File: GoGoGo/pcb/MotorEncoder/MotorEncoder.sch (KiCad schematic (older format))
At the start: 7 parts

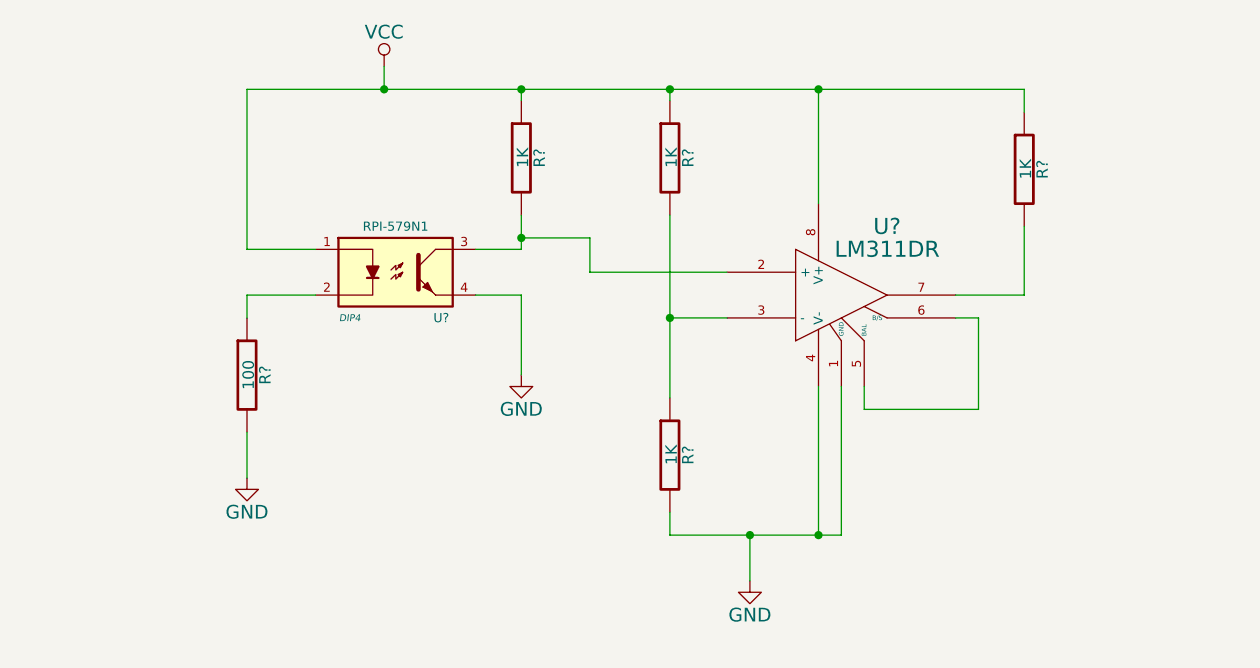
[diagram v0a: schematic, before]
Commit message: GGG MotorEncoder schematic updated with missing video items
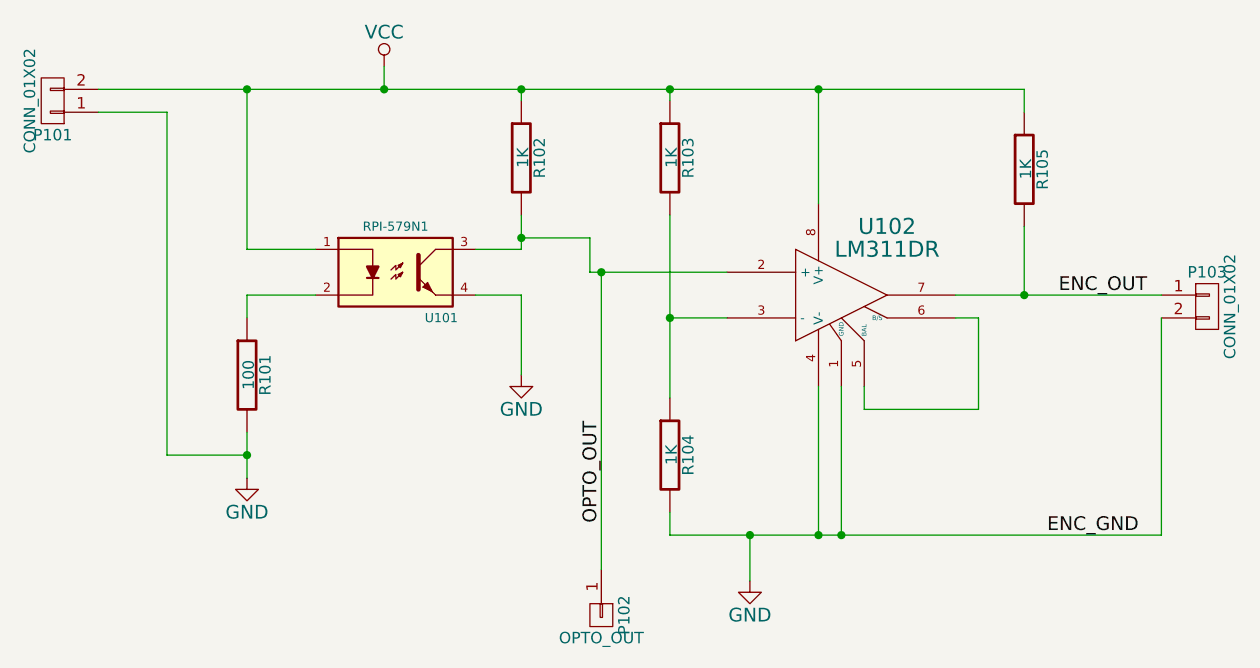
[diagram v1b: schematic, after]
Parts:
- added P101, P103: CONN_01X02, symbol CONN_01X02
- added P102: OPTO_OUT, symbol CONN_01X01
- R101, R102, R103, R104, R105: renamed from R?; footprint (none) -> Resistors_SMD:R_0805_HandSoldering
- U101: renamed from U?; footprint DIP4 -> (none)
- gave numbers to parts that had none: 1
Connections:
- net GND: now also P101.1 (P1), P103.2 (P2)
- net VCC: now also P101.2 (P2)
- net OPTO_OUT: now reaches R102.2, U101.3, U102.2 (+)
- net OPTO_OUT: now also P102.1 (P1)
- net ENC_OUT: now reaches R105.2, U102.7
- net ENC_OUT: now also P103.1 (P1)
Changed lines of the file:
@@
 $EndDescr
 $Comp
-L RPI-579N1 U?
+L RPI-579N1 U101
 U 1 1 55B03B5A
 P 5550 3350
-F 0 "U?" H 5750 3150 40  0000 C CNN
+F 0 "U101" H 5750 3150 40  0000 C CNN
 F 1 "RPI-579N1" H 5550 3550 40  0000 C CNN
-F 2 "DIP4" H 5350 3150 30  0000 C CIN
+F 2 "" H 5350 3150 30  0000 C CIN
 F 3 "" H 5550 3350 60  0000 C CNN
 	1    5550 3350
@@
 $EndComp
 $Comp
-L R R?
+L R R101
 U 1 1 55B03C1A
 P 4900 3800
-F 0 "R?" V 4980 3800 50  0000 C CNN
+F 0 "R101" V 4980 3800 50  0000 C CNN
 F 1 "100" V 4907 3801 50  0000 C CNN
-F 2 "" V 4830 3800 30  0000 C CNN
+F 2 "Resistors_SMD:R_0805_HandSoldering" V 4830 3800 30  0001 C CNN
 F 3 "" H 4900 3800 30  0000 C CNN
 	1    4900 3800
@@
 $EndComp
 $Comp
-L VCC #PWR?
+L VCC #PWR102
 U 1 1 55B03C53
 P 5500 2450
-F 0 "#PWR?" H 5500 2300 60  0001 C CNN
+F 0 "#PWR102" H 5500 2300 60  0001 C CNN
 F 1 "VCC" H 5500 2600 60  0000 C CNN
 F 2 "" H 5500 2450 60  0000 C CNN
@@
 $EndComp
 $Comp
-L GND #PWR?
+L GND #PWR101
 U 1 1 55B03C96
 P 4900 4250
-F 0 "#PWR?" H 4900 4000 60  0001 C CNN
+F 0 "#PWR101" H 4900 4000 60  0001 C CNN
 F 1 "GND" H 4900 4100 60  0000 C CNN
 F 2 "" H 4900 4250 60  0000 C CNN
@@
 $EndComp
 $Comp
-L GND #PWR?
+L GND #PWR103
 U 1 1 55B03CB8
 P 6100 3800
-F 0 "#PWR?" H 6100 3550 60  0001 C CNN
+F 0 "#PWR103" H 6100 3550 60  0001 C CNN
 F 1 "GND" H 6100 3650 60  0000 C CNN
 F 2 "" H 6100 3800 60  0000 C CNN
@@
 $EndComp
 $Comp
-L LM311N U?
+L LM311N U102
 U 1 1 55B040EE
 P 7500 3450
-F 0 "U?" H 7700 3750 70  0000 C CNN
+F 0 "U102" H 7700 3750 70  0000 C CNN
 F 1 "LM311DR" H 7700 3650 70  0000 C CNN
-F 2 "" H 7500 3450 60  0000 C CNN
+F 2 "" H 7500 3450 60  0001 C CNN
 F 3 "" H 7500 3450 60  0000 C CNN
 	1    7500 3450
@@
 	6100 3250 6100 3100
 Wire Wire Line
-	4900 2550 8300 2550
+	4250 2550 8300 2550
 Wire Wire Line
 	6100 2550 6100 2600
@@
 Connection ~ 6100 2550
 $Comp
-L R R?
+L R R103
 U 1 1 55B04354
 P 6750 2850
-F 0 "R?" V 6830 2850 50  0000 C CNN
+F 0 "R103" V 6830 2850 50  0000 C CNN
 F 1 "1K" V 6757 2851 50  0000 C CNN
-F 2 "" V 6680 2850 30  0000 C CNN
+F 2 "Resistors_SMD:R_0805_HandSoldering" V 6680 2850 30  0001 C CNN
 F 3 "" H 6750 2850 30  0000 C CNN
 	1    6750 2850
@@
 	6750 3550 7000 3550
 $Comp
-L R R?
+L R R104
 U 1 1 55B043E5
 P 6750 4150
-F 0 "R?" V 6830 4150 50  0000 C CNN
+F 0 "R104" V 6830 4150 50  0000 C CNN
 F 1 "1K" V 6757 4151 50  0000 C CNN
-F 2 "" V 6680 4150 30  0000 C CNN
+F 2 "Resistors_SMD:R_0805_HandSoldering" V 6680 4150 30  0001 C CNN
 F 3 "" H 6750 4150 30  0000 C CNN
 	1    6750 4150
@@
 Connection ~ 7400 2550
 Wire Wire Line
-	8000 3450 8300 3450
-$Comp
-L R R?
+	8000 3450 8900 3450
+$Comp
+L R R105
 U 1 1 55B044E9
 P 8300 2900
-F 0 "R?" V 8380 2900 50  0000 C CNN
+F 0 "R105" V 8380 2900 50  0000 C CNN
 F 1 "1K" V 8307 2901 50  0000 C CNN
-F 2 "" V 8230 2900 30  0000 C CNN
+F 2 "Resistors_SMD:R_0805_HandSoldering" V 8230 2900 30  0001 C CNN
 F 3 "" H 8300 2900 30  0000 C CNN
 	1    8300 2900
@@
 	6750 4400 6750 4500
 Wire Wire Line
-	6750 4500 7500 4500
+	6750 4500 8900 4500
 Wire Wire Line
 	7500 4500 7500 3850
@@
 Connection ~ 7100 4500
 $Comp
-L GND #PWR?
+L GND #PWR104
 U 1 1 55B046A7
 P 7100 4700
-F 0 "#PWR?" H 7100 4450 60  0001 C CNN
+F 0 "#PWR104" H 7100 4450 60  0001 C CNN
 F 1 "GND" H 7100 4550 60  0000 C CNN
 F 2 "" H 7100 4700 60  0000 C CNN
@@
 $EndComp
 $Comp
-L R R?
+L R R102
 U 1 1 55B04737
 P 6100 2850
-F 0 "R?" V 6180 2850 50  0000 C CNN
+F 0 "R102" V 6180 2850 50  0000 C CNN
 F 1 "1K" V 6107 2851 50  0000 C CNN
-F 2 "" V 6030 2850 30  0000 C CNN
+F 2 "Resistors_SMD:R_0805_HandSoldering" V 6030 2850 30  0001 C CNN
 F 3 "" H 6100 2850 30  0000 C CNN
 	1    6100 2850
 	1    0    0    -1
 $EndComp
+$Comp
+L CONN_01X02 P101
+U 1 1 55B047FC
+P 4050 2600
+F 0 "P101" H 4050 2750 50  0000 C CNN
+F 1 "CONN_01X02" V 4150 2600 50  0000 C CNN
+F 2 "" H 4050 2600 60  0000 C CNN
+F 3 "" H 4050 2600 60  0000 C CNN
+	1    4050 2600
+	-1   0    0    1
+$EndComp
+Wire Wire Line
+	4250 2650 4550 2650
+Wire Wire Line
+	4550 2650 4550 4150
+Wire Wire Line
+	4550 4150 4900 4150
+Connection ~ 4900 4150
+Connection ~ 4900 2550
+Connection ~ 8300 3450
+Wire Wire Line
+	8900 4500 8900 3550
+Connection ~ 7500 4500
+$Comp
+L CONN_01X02 P103
+U 1 1 55B04BA9
+P 9100 3500
+F 0 "P103" H 9100 3650 50  0000 C CNN
+F 1 "CONN_01X02" V 9200 3500 50  0000 C CNN
+F 2 "" H 9100 3500 60  0000 C CNN
+F 3 "" H 9100 3500 60  0000 C CNN
+	1    9100 3500
+	1    0    0    -1
+$EndComp
+Wire Wire Line
+	6450 3350 6450 4650
+Connection ~ 6450 3350
+$Comp
+L CONN_01X01 P102
+U 1 1 55B04D73
+P 6450 4850
+F 0 "P102" H 6450 4950 50  0000 C CNN
+F 1 "OPTO_OUT" V 6550 4850 50  0000 C CNN
+F 2 "" H 6450 4850 60  0000 C CNN
+F 3 "" H 6450 4850 60  0000 C CNN
+	1    6450 4850
+	0    1    1    0
+$EndComp
+Text Label 8450 3450 0    60   ~ 0
+ENC_OUT
+Text Label 6450 4000 3    60   ~ 0
+OPTO_OUT
+Text Label 8400 4500 0    60   ~ 0
+ENC_GND
 $EndSCHEMATC

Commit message: GGG MotorEncoder begin to associate footprints
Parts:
- P101, P103: footprint (none) -> Pin_Headers:Pin_Header_Straight_1x02
- P102: footprint (none) -> pcb:TESTPOINT_1
- U102: footprint (none) -> Housings_SOIC:SOIC-8_3.9x4.9mm_Pitch1.27mm
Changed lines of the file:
@@
 F 0 "U101" H 5750 3150 40  0000 C CNN
 F 1 "RPI-579N1" H 5550 3550 40  0000 C CNN
-F 2 "" H 5350 3150 30  0000 C CIN
+F 2 "" H 5350 3150 30  0001 C CIN
 F 3 "" H 5550 3350 60  0000 C CNN
 	1    5550 3350
@@
 $EndComp
 $Comp
-L VCC #PWR102
+L VCC #PWR01
 U 1 1 55B03C53
 P 5500 2450
-F 0 "#PWR102" H 5500 2300 60  0001 C CNN
+F 0 "#PWR01" H 5500 2300 60  0001 C CNN
 F 1 "VCC" H 5500 2600 60  0000 C CNN
 F 2 "" H 5500 2450 60  0000 C CNN
@@
 $EndComp
 $Comp
-L GND #PWR101
+L GND #PWR02
 U 1 1 55B03C96
 P 4900 4250
-F 0 "#PWR101" H 4900 4000 60  0001 C CNN
+F 0 "#PWR02" H 4900 4000 60  0001 C CNN
 F 1 "GND" H 4900 4100 60  0000 C CNN
 F 2 "" H 4900 4250 60  0000 C CNN
@@
 $EndComp
 $Comp
-L GND #PWR103
+L GND #PWR03
 U 1 1 55B03CB8
 P 6100 3800
-F 0 "#PWR103" H 6100 3550 60  0001 C CNN
+F 0 "#PWR03" H 6100 3550 60  0001 C CNN
 F 1 "GND" H 6100 3650 60  0000 C CNN
 F 2 "" H 6100 3800 60  0000 C CNN
@@
 F 0 "U102" H 7700 3750 70  0000 C CNN
 F 1 "LM311DR" H 7700 3650 70  0000 C CNN
-F 2 "" H 7500 3450 60  0001 C CNN
+F 2 "Housings_SOIC:SOIC-8_3.9x4.9mm_Pitch1.27mm" H 7500 3450 60  0001 C CNN
 F 3 "" H 7500 3450 60  0000 C CNN
 	1    7500 3450
@@
 Connection ~ 7100 4500
 $Comp
-L GND #PWR104
+L GND #PWR04
 U 1 1 55B046A7
 P 7100 4700
-F 0 "#PWR104" H 7100 4450 60  0001 C CNN
+F 0 "#PWR04" H 7100 4450 60  0001 C CNN
 F 1 "GND" H 7100 4550 60  0000 C CNN
 F 2 "" H 7100 4700 60  0000 C CNN
@@
 F 0 "P101" H 4050 2750 50  0000 C CNN
 F 1 "CONN_01X02" V 4150 2600 50  0000 C CNN
-F 2 "" H 4050 2600 60  0000 C CNN
+F 2 "Pin_Headers:Pin_Header_Straight_1x02" H 4050 2600 60  0001 C CNN
 F 3 "" H 4050 2600 60  0000 C CNN
 	1    4050 2600
@@
 F 0 "P103" H 9100 3650 50  0000 C CNN
 F 1 "CONN_01X02" V 9200 3500 50  0000 C CNN
-F 2 "" H 9100 3500 60  0000 C CNN
+F 2 "Pin_Headers:Pin_Header_Straight_1x02" H 9100 3500 60  0001 C CNN
 F 3 "" H 9100 3500 60  0000 C CNN
 	1    9100 3500
@@
 F 0 "P102" H 6450 4950 50  0000 C CNN
 F 1 "OPTO_OUT" V 6550 4850 50  0000 C CNN
-F 2 "" H 6450 4850 60  0000 C CNN
+F 2 "pcb:TESTPOINT_1" H 6450 4850 60  0001 C CNN
 F 3 "" H 6450 4850 60  0000 C CNN
 	1    6450 4850

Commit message: GGG MotorEncoder imported testpoint footprint
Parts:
- U101: footprint (none) -> pcb:RPI-579N1
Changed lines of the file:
@@
 F 0 "U101" H 5750 3150 40  0000 C CNN
 F 1 "RPI-579N1" H 5550 3550 40  0000 C CNN
-F 2 "" H 5350 3150 30  0001 C CIN
+F 2 "pcb:RPI-579N1" H 5350 3150 30  0001 C CIN
 F 3 "" H 5550 3350 60  0000 C CNN
 	1    5550 3350

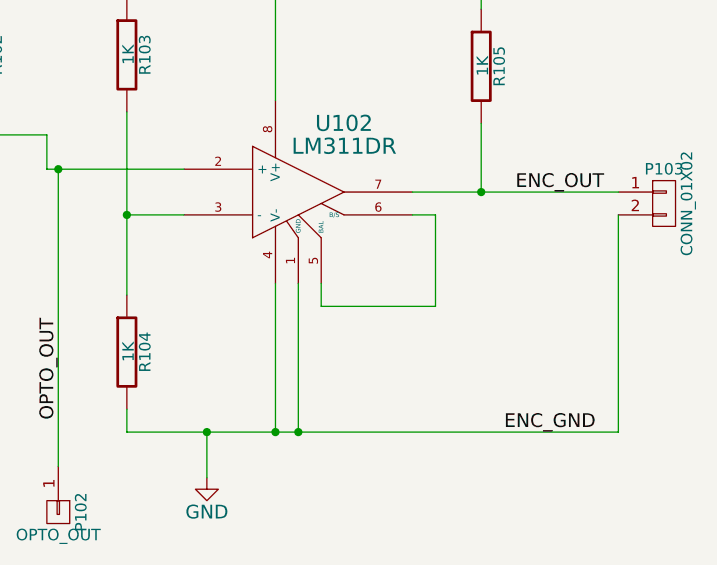
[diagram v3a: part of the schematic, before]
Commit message: GGG MotorEncoder final pcb submitted to OSH Park
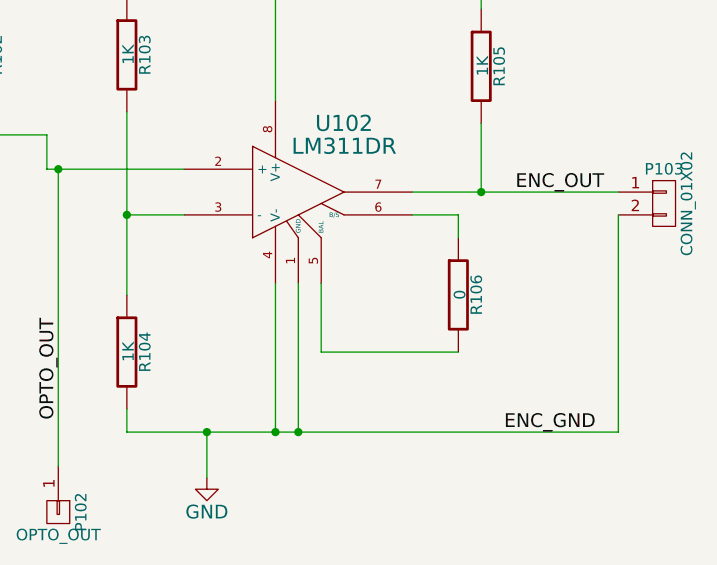
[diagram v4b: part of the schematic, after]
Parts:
- added R106: 0, Resistors_SMD:R_0805_HandSoldering, symbol R
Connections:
- net at U102.5 (BAL): now also R106.2; no longer U102.6 (B/S)
- new net: R106.1, U102.6 (B/S)
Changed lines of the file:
@@
 	8300 2550 8300 2650
 Wire Wire Line
-	8000 3550 8100 3550
+	8000 3550 8200 3550
 Wire Wire Line
-	8100 3550 8100 3950
-Wire Wire Line
-	8100 3950 7600 3950
-Wire Wire Line
-	7600 3950 7600 3850
+	7600 3850 7600 4150
 Wire Wire Line
 	6750 4400 6750 4500
@@
 Text Label 8400 4500 0    60   ~ 0
 ENC_GND
+$Comp
+L R R106
+U 1 1 55B06538
+P 8200 3900
+F 0 "R106" V 8280 3900 50  0000 C CNN
+F 1 "0" V 8207 3901 50  0000 C CNN
+F 2 "Resistors_SMD:R_0805_HandSoldering" V 8130 3900 30  0001 C CNN
+F 3 "" H 8200 3900 30  0000 C CNN
+	1    8200 3900
+	1    0    0    -1
+$EndComp
+Wire Wire Line
+	8200 3550 8200 3650
+Wire Wire Line
+	7600 4150 8200 4150
 $EndSCHEMATC

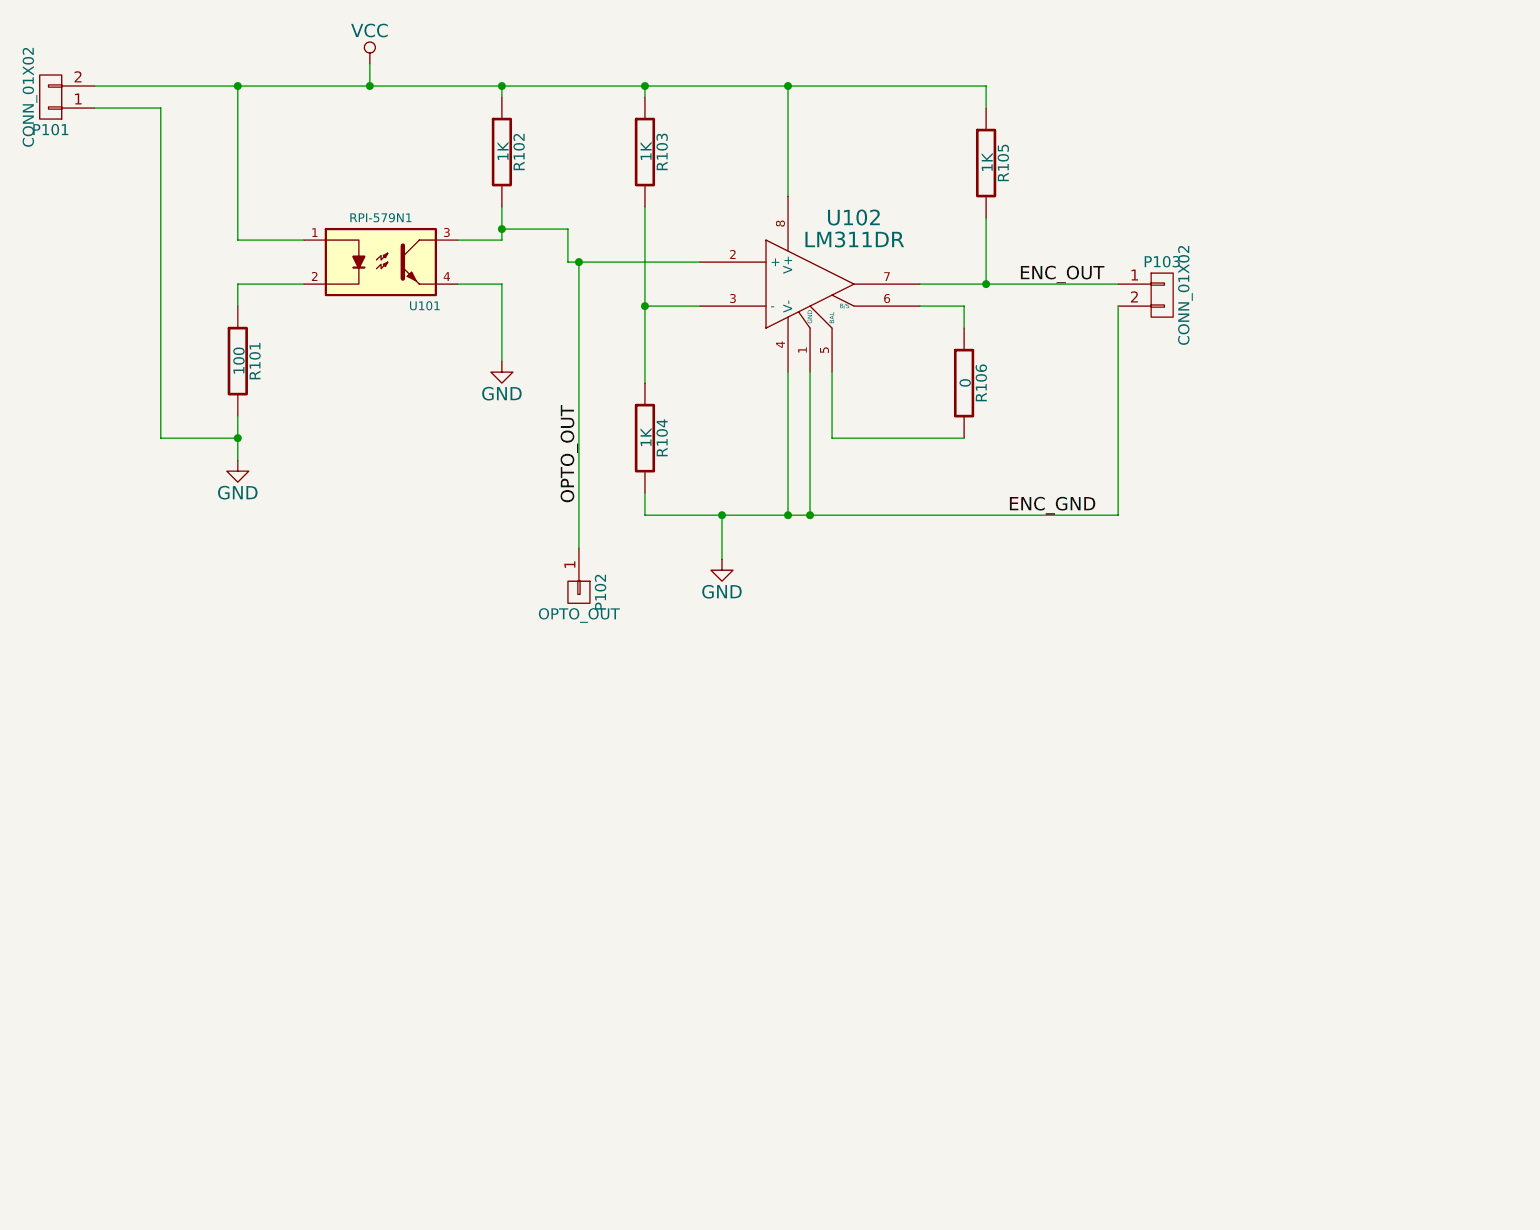
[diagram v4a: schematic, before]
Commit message: GGG : Motor Encoder : changed R102 to 10K and started v2
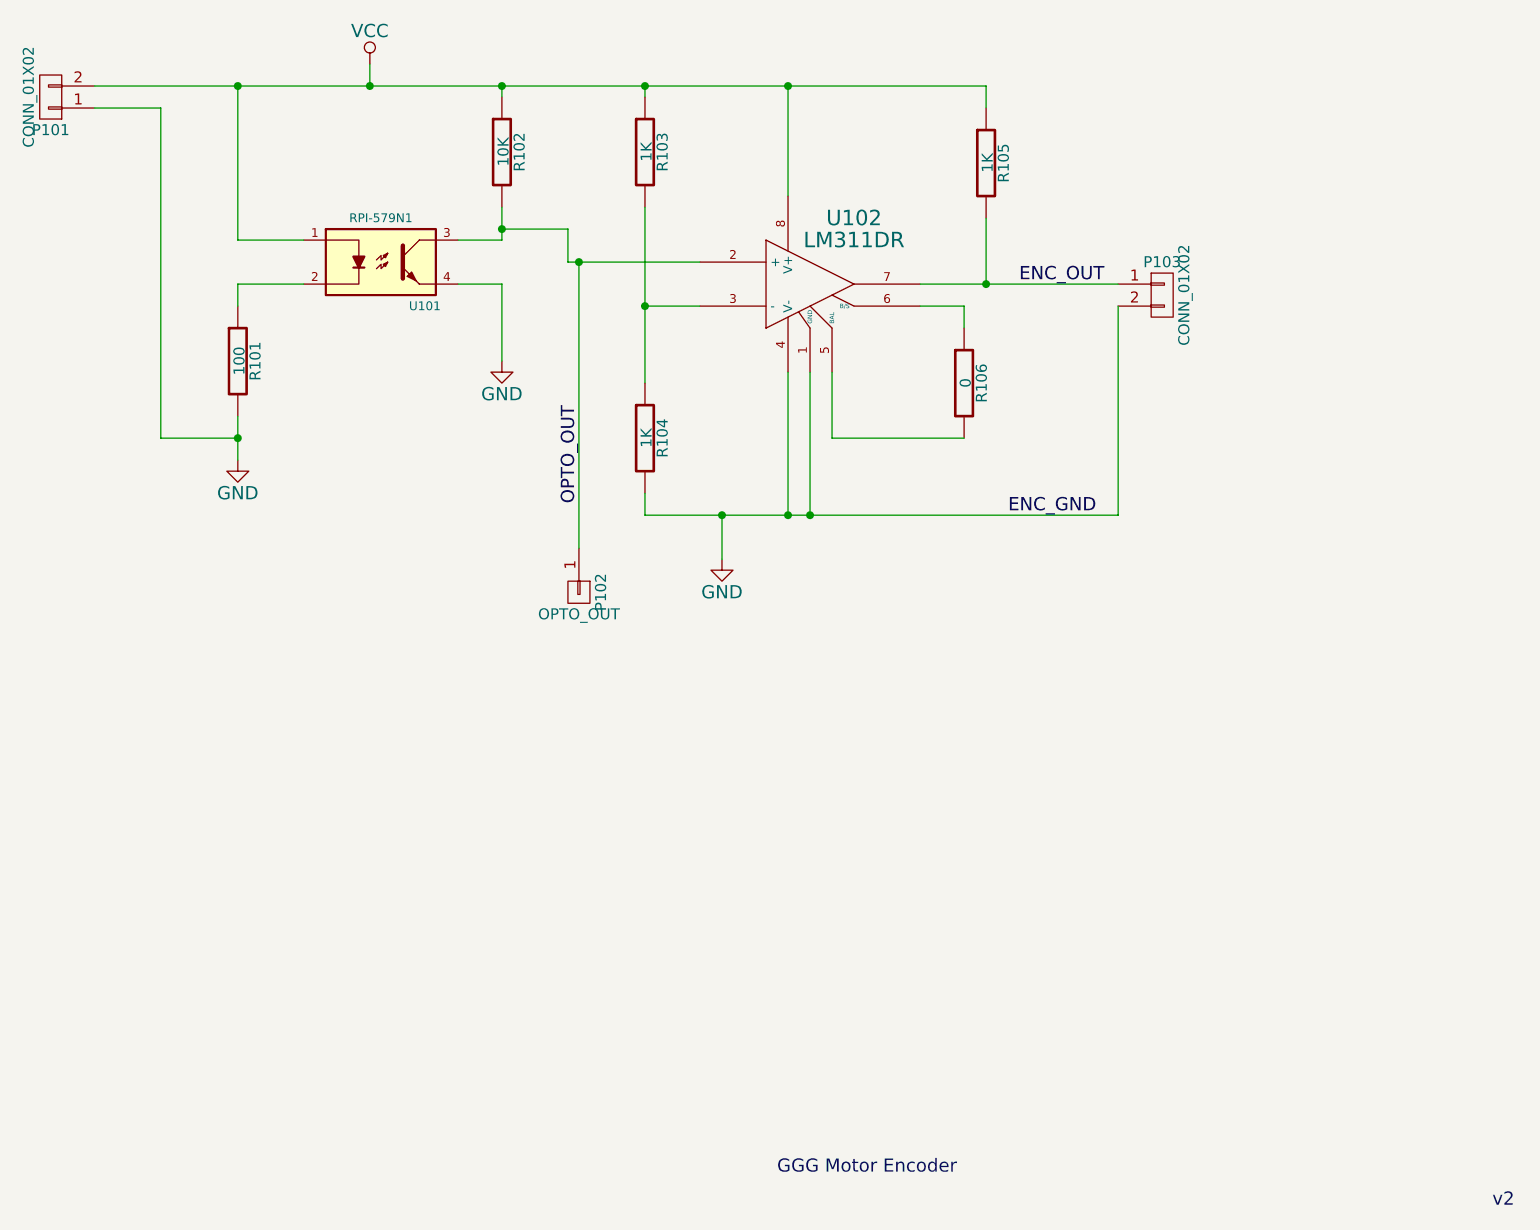
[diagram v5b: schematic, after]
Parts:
- R102: value 1K -> 10K
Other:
- note added: "GGG Motor Encoder"
- note added: "v2"
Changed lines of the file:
@@
 P 6100 2850
 F 0 "R102" V 6180 2850 50  0000 C CNN
-F 1 "1K" V 6107 2851 50  0000 C CNN
+F 1 "10K" V 6107 2851 50  0000 C CNN
 F 2 "Resistors_SMD:R_0805_HandSoldering" V 6030 2850 30  0001 C CNN
 F 3 "" H 6100 2850 30  0000 C CNN
@@
 Wire Wire Line
 	7600 4150 8200 4150
+Text Notes 7350 7500 0    60   ~ 0
+GGG Motor Encoder
+Text Notes 10600 7650 0    60   ~ 0
+v2
 $EndSCHEMATC
